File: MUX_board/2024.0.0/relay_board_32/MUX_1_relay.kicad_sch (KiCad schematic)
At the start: 4 parts, among them K5 G5LE-1-VD, Q5 STP16NF06L

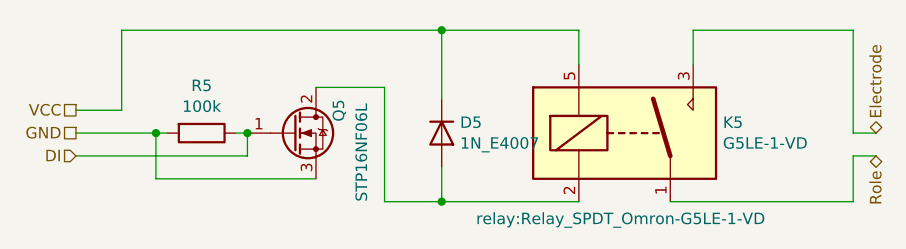
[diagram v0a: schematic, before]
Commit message: adds filtering capacitors on MCP23017
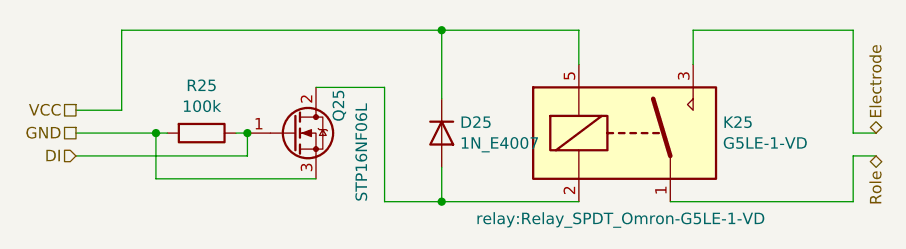
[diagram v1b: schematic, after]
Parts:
- renumbered D5 to D25, K5 to K25, Q5 to Q25, R5 to R25
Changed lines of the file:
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@@
   (symbol (lib_id "Diode:1N4007") (at 127 115.57 270)
     (in_bom yes) (on_board yes)
-    (property "Reference" "D5" (id 0) (at 129.032 114.4016 90)
+    (property "Reference" "D25" (id 0) (at 129.032 114.4016 90)
       (effects (font (size 1.27 1.27)) (justify left))
     )
@@
   (symbol (lib_id "relay_card_single:G5LE-1-VD") (at 147.32 115.57 0)
     (in_bom yes) (on_board yes)
-    (property "Reference" "K5" (id 0) (at 158.242 114.4016 0)
+    (property "Reference" "K25" (id 0) (at 158.242 114.4016 0)
       (effects (font (size 1.27 1.27)) (justify left))
     )
@@
   (symbol (lib_id "relay_card_single:STP16NF06L") (at 110.49 115.57 0)
     (in_bom yes) (on_board yes)
-    (property "Reference" "Q5" (id 0) (at 115.57 114.3 90)
+    (property "Reference" "Q25" (id 0) (at 115.57 114.3 90)
       (effects (font (size 1.27 1.27)) (justify left))
     )
@@
   (symbol (lib_id "Device:R") (at 100.33 115.57 270)
     (in_bom yes) (on_board yes)
-    (property "Reference" "R5" (id 0) (at 100.33 110.3122 90))
+    (property "Reference" "R25" (id 0) (at 100.33 110.3122 90))
     (property "Value" "100k" (id 1) (at 100.33 112.6236 90))
     (property "Footprint" "Resistor_THT:R_Axial_DIN0207_L6.3mm_D2.5mm_P15.24mm_Horizontal" (id 2) (at 100.33 113.792 90)
